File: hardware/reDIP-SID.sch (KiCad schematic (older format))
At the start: 72 parts, among them J1 Conn_01x01, J2 Conn_01x05, J3 Conn_01x14, J4 Conn_01x10, J5 TYPE-C-31-M-12, J6 Conn_02x05_Odd_Even, SW1 KXT311LHS, U1 NCP115AMX120TCG, U10 W25Q128JVPIM, U11 ICE40UP5K-SG48I, U2 NCP167AMX330TBG, U3 NCP115AMX120TCG, U4 FPF1321UCX, U5 SN74CBTD16211DGVR, U6 SGTL5000XNLA3, U7 NUF2042XV6, U8 MCP6H01T-E/OT, U9 LY68L6400SLIT, X1 ASCO-24.000MHZ-EK-T3

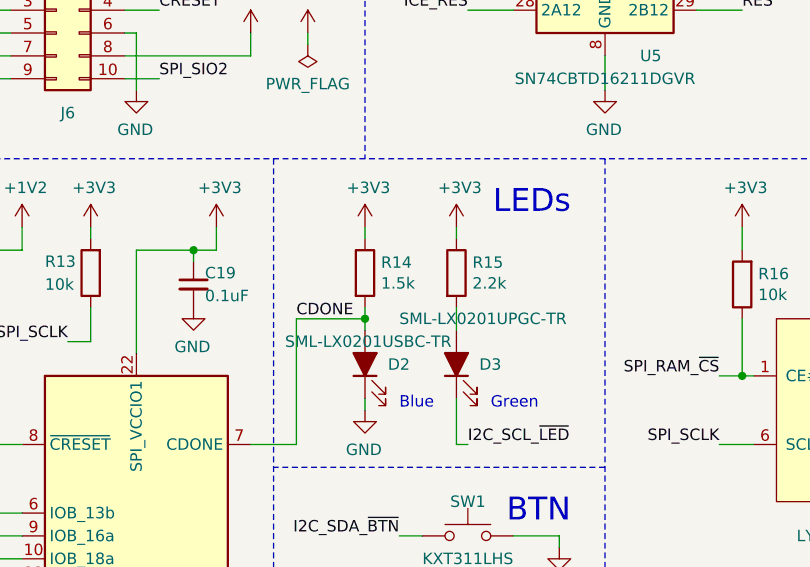
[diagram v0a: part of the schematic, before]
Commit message: Minor updates
* Dimmer blue CDONE LED
* BOM QA
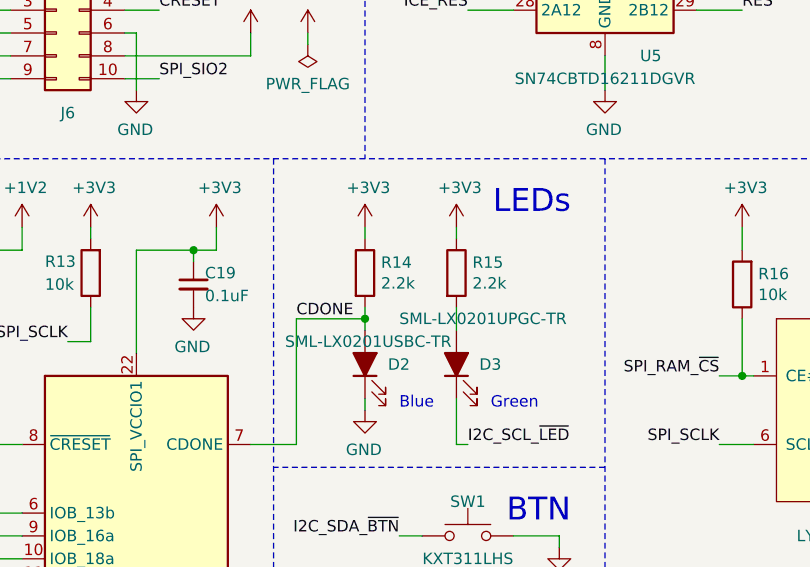
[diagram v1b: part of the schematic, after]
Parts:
- R14: value 1.5k -> 2.2k; Description RES 1.5kΩ 50mW 5% 0201 -> RES 2.2kΩ 50mW 5% 0201; PN ERJ-1GNJ152C -> ERJ-1GNJ222C
- R20: Description RES 22Ω 50mW 5% 0201 -> RES 22Ω 50mW 1% 0201; PN ERJ-1GNJ220C -> ERJ-1GNF22R0C
- SW1: Description SW TACT 3.0 x 2.0 mm -> SW TACT 100gf 3.0x2.0 mm
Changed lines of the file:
@@
 F 1 "W25Q128JVPIM" H 10200 5000 50  0000 C CNN
 F 2 "Package_SON:WSON-8-1EP_6x5mm_P1.27mm_EP3.4x4.3mm" H 10200 5600 50  0001 C CNN
-F 3 "https://www.winbond.com/resource-files/w25q128jv%20revf%2003272018%20plus.pdf" H 10200 5600 50  0001 C CNN
+F 3 "https://www.winbond.com/resource-files/W25Q128JV%20RevH%2003102021%20Plus.pdf" H 10200 5600 50  0001 C CNN
 F 4 "IC FLASH 128Mbit WSON-8" H 10200 5600 50  0001 C CNN "Description"
 F 5 "Winbond" H 10200 5600 50  0001 C CNN "Mfg"
@@
 P 5900 5050
 F 0 "R14" H 5970 5096 50  0000 L CNN
-F 1 "1.5k" H 5970 5005 50  0000 L CNN
+F 1 "2.2k" H 5970 5005 50  0000 L CNN
 F 2 "Resistor_SMD:R_0201_0603Metric" V 5830 5050 50  0001 C CNN
-F 3 "https://industrial.panasonic.com/ww/products/pt/general-purpose-chip-resistors/models/ERJ1GNJ152C" H 5900 5050 50  0001 C CNN
-F 4 "RES 1.5kΩ 50mW 5% 0201" H 5900 5050 50  0001 C CNN "Description"
+F 3 "https://industrial.panasonic.com/ww/products/pt/general-purpose-chip-resistors/models/ERJ1GNJ222C" H 5900 5050 50  0001 C CNN
+F 4 "RES 2.2kΩ 50mW 5% 0201" H 5900 5050 50  0001 C CNN "Description"
 F 5 "Panasonic" H 5900 5050 50  0001 C CNN "Mfg"
-F 6 "ERJ-1GNJ152C" H 5900 5050 50  0001 C CNN "PN"
+F 6 "ERJ-1GNJ222C" H 5900 5050 50  0001 C CNN "PN"
 	1    5900 5050
 	1    0    0    -1
@@
 F 1 "Conn_02x05_Odd_Even" H 4600 4326 50  0001 C CNN
 F 2 "reDIP:PinHeader_2x05_P2.54mm_Vertical" H 4550 4000 50  0001 C CNN
-F 3 "https://drawings-pdf.s3.amazonaws.com/11636.pdf" H 4550 4000 50  0001 C CNN
+F 3 "" H 4550 4000 50  0001 C CNN
 F 4 "CONN HDR SQ PIN 2x5 POS .100\" GOLD MATING 6mm TAIL 3mm" H 4550 4000 50  0001 C CNN "Description"
 F 5 "" H 4550 4000 50  0001 C CNN "Mfg"
@@
 F 1 "NCP167AMX330TBG" H 4050 1374 50  0000 C CNN
 F 2 "ONSemi:CASE_711AJ_1.0x1.0mm_P0.65mm" H 4050 1100 50  0001 C CNN
-F 3 "https://www.onsemi.com/pub/Collateral/NCP167-D.PDF" H 4050 1100 50  0001 C CNN
+F 3 "https://www.onsemi.com/pdf/datasheet/ncp167-d.pdf" H 4050 1100 50  0001 C CNN
 F 4 "onsemi" H 4050 1100 50  0001 C CNN "Mfg"
 F 5 "NCP167AMX330TBG" H 4050 1100 50  0001 C CNN "PN"
@@
 F 2 "CK:SW_SPST_CK_KXT3" H 6350 6400 50  0001 C CNN
 F 3 "https://www.ckswitches.com/media/1465/kxt3.pdf" H 6350 6400 50  0001 C CNN
-F 4 "SW TACT 3.0 x 2.0 mm" H 6350 6200 50  0001 C CNN "Description"
+F 4 "SW TACT 100gf 3.0x2.0 mm" H 6350 6200 50  0001 C CNN "Description"
 F 5 "C&K" H 6350 6200 50  0001 C CNN "Mfg"
 F 6 "KXT311LHS" H 6350 6200 50  0001 C CNN "PN"
@@
 F 1 "22" V 4200 7400 50  0000 C CNN
 F 2 "Resistor_SMD:R_0201_0603Metric" H 4250 7300 50  0001 C CNN
-F 3 "https://industrial.panasonic.com/ww/products/pt/general-purpose-chip-resistors/models/ERJ1GNJ220C" H 4250 7300 50  0001 C CNN
+F 3 "https://industrial.panasonic.com/ww/products/pt/general-purpose-chip-resistors/models/ERJ1GNF22R0C" H 4250 7300 50  0001 C CNN
 F 4 "Panasonic" H 4250 7300 50  0001 C CNN "Mfg"
-F 5 "ERJ-1GNJ220C" H 4250 7300 50  0001 C CNN "PN"
-F 6 "RES 22Ω 50mW 5% 0201" H 4250 7300 50  0001 C CNN "Description"
+F 5 "ERJ-1GNF22R0C" H 4250 7300 50  0001 C CNN "PN"
+F 6 "RES 22Ω 50mW 1% 0201" H 4250 7300 50  0001 C CNN "Description"
 	1    4250 7300
 	0    1    1    0
@@
 F 1 "NUF2042XV6" H 2600 2800 50  0000 C CNN
 F 2 "ONSemi:CASE_463A_1.6x1.2mm_P0.5mm" H 2600 2750 50  0001 C CNN
-F 3 "https://www.onsemi.com/pub/Collateral/NUF2030XV6-D.PDF" H 2800 3600 50  0001 C CNN
+F 3 "https://www.onsemi.com/pdf/datasheet/nuf2030xv6-d.pdf" H 2800 3600 50  0001 C CNN
 F 4 "IC USB TERMINATOR ESD PROTECTION SOT-563" H 2600 3250 50  0001 C CNN "Description"
 F 5 "onsemi" H 2600 3250 50  0001 C CNN "Mfg"

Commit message: Tweaks before manufacture
* Added test point for 5V rail
* Got rid of one BOM line by changing the MIC voltage divider
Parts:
- removed TP1, TP2: TestPoint_Flag, reDIP:TestPoint_Pad_D0.75mm, symbol Connector:TestPoint_Flag
- added TP1, TP2, TP3: TestPoint, reDIP:TestPoint_Pad_D0.75mm, symbol Connector:TestPoint
- R5: value 402k -> 100k; Description RES 402kΩ 50mW 1% 0201 -> RES 100kΩ 50mW 1% 0201; PN ERJ-1GNF4023C -> ERJ-1GNF1003C
- R8: value 100k -> 20k; Description RES 100kΩ 50mW 1% 0201 -> RES 20kΩ 50mW 1% 0201; PN ERJ-1GNF1003C -> ERJ-1GNF2002C
- renumbered TP3 to TP4, TP4 to TP5
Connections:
- net +1V2: now also TP2.1
- net +5V: now also TP1.1
- net VDDD: now also TP3.1
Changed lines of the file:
@@
 Sheet 1 1
 Title "reDIP SID"
-Date "2021-08-28"
+Date "2021-09-07"
 Rev "1.0"
 Comp "Nimrod"
@@
 $EndComp
 $Comp
-L Connector:TestPoint_Flag TP4
+L Connector:TestPoint_Flag TP5
 U 1 1 5EBD10F6
 P 10700 1650
-F 0 "TP4" H 10960 1698 50  0000 L CNN
+F 0 "TP5" H 10960 1698 50  0000 L CNN
 F 1 "TestPoint_Flag" H 10960 1653 50  0001 L CNN
 F 2 "reDIP:TestPoint_Pad_D0.75mm" H 10900 1650 50  0001 C CNN
@@
 $EndComp
 $Comp
-L Connector:TestPoint_Flag TP3
+L Connector:TestPoint_Flag TP4
 U 1 1 5EA8BEE8
 P 10700 1500
-F 0 "TP3" H 10960 1548 50  0000 L CNN
+F 0 "TP4" H 10960 1548 50  0000 L CNN
 F 1 "TestPoint_Flag" H 10960 1503 50  0001 L CNN
 F 2 "reDIP:TestPoint_Pad_D0.75mm" H 10900 1500 50  0001 C CNN
@@
 Power
 Wire Wire Line
-	3250 1000 3250 800
+	3250 1000 3250 850
 Wire Wire Line
 	4550 1000 4550 800
@@
 Wire Wire Line
 	3950 3450 3950 3500
-Wire Wire Line
-	3150 1200 3250 1200
 $Comp
 L Device:C_Small C4
@@
 Connection ~ 5750 6850
 Wire Wire Line
-	5600 1000 5600 800
+	5600 1000 5600 850
 Wire Wire Line
 	5500 1000 5600 1000
@@
 Connection ~ 4750 1000
 $Comp
-L Connector:TestPoint_Flag TP2
-U 1 1 615B5C23
-P 5600 1200
-F 0 "TP2" H 5850 1200 50  0000 R CNN
-F 1 "TestPoint_Flag" H 5860 1203 50  0001 L CNN
-F 2 "reDIP:TestPoint_Pad_D0.75mm" H 5800 1200 50  0001 C CNN
-F 3 "~" H 5800 1200 50  0001 C CNN
-F 4 "PAD" H 5600 1200 50  0001 C CNN "DNP"
-	1    5600 1200
-	1    0    0    1
-$EndComp
-$Comp
 L Device:C_Small C8
 U 1 1 615B5C31
@@
 	1    0    0    -1
 $EndComp
-$Comp
-L Connector:TestPoint_Flag TP1
-U 1 1 5F4F3F1B
-P 3250 1200
-F 0 "TP1" H 3500 1200 50  0000 R CNN
-F 1 "TestPoint_Flag" H 3510 1203 50  0001 L CNN
-F 2 "reDIP:TestPoint_Pad_D0.75mm" H 3450 1200 50  0001 C CNN
-F 3 "~" H 3450 1200 50  0001 C CNN
-F 4 "PAD" H 3250 1200 50  0001 C CNN "DNP"
-	1    3250 1200
-	1    0    0    1
-$EndComp
 Wire Wire Line
 	3150 1000 3150 1100
@@
 	3150 1100 3150 1200
 Connection ~ 4550 1000
-Connection ~ 3150 1200
 Wire Wire Line
 	8250 1450 8250 1500
@@
 	5500 1000 5500 1200
 Wire Wire Line
-	5600 1200 5500 1200
-Connection ~ 5500 1200
-Wire Wire Line
 	10100 3500 10100 3750
 Wire Wire Line
@@
 	1450 1300 1450 1450
 Wire Wire Line
-	2200 800  2200 1000
+	2200 800  2200 850
 $Comp
 L Device:R R5
@@
 P 8450 2600
 F 0 "R5" V 8400 2500 50  0000 R CNN
-F 1 "402k" V 8400 2900 50  0000 R CNN
+F 1 "100k" V 8400 2900 50  0000 R CNN
 F 2 "Resistor_SMD:R_0201_0603Metric" V 8380 2600 50  0001 C CNN
-F 3 "https://industrial.panasonic.com/ww/products/pt/general-purpose-chip-resistors/models/ERJ1GNF4023C" H 8450 2600 50  0001 C CNN
+F 3 "https://industrial.panasonic.com/ww/products/pt/general-purpose-chip-resistors/models/ERJ1GNF1003C" H 8450 2600 50  0001 C CNN
 F 4 "Panasonic" H 8450 2600 50  0001 C CNN "Mfg"
-F 5 "ERJ-1GNF4023C" H 8450 2600 50  0001 C CNN "PN"
-F 6 "RES 402kΩ 50mW 1% 0201" H 8450 2600 50  0001 C CNN "Description"
+F 5 "ERJ-1GNF1003C" H 8450 2600 50  0001 C CNN "PN"
+F 6 "RES 100kΩ 50mW 1% 0201" H 8450 2600 50  0001 C CNN "Description"
 	1    8450 2600
 	0    1    1    0
@@
 P 8450 2750
 F 0 "R8" V 8400 2650 50  0000 R CNN
-F 1 "100k" V 8400 3050 50  0000 R CNN
+F 1 "20k" V 8400 3050 50  0000 R CNN
 F 2 "Resistor_SMD:R_0201_0603Metric" V 8380 2750 50  0001 C CNN
-F 3 "https://industrial.panasonic.com/ww/products/pt/general-purpose-chip-resistors/models/ERJ1GNF1003C" H 8450 2750 50  0001 C CNN
+F 3 "https://industrial.panasonic.com/ww/products/pt/general-purpose-chip-resistors/models/ERJ1GNF2002C" H 8450 2750 50  0001 C CNN
 F 4 "Panasonic" H 8450 2750 50  0001 C CNN "Mfg"
-F 5 "ERJ-1GNF1003C" H 8450 2750 50  0001 C CNN "PN"
-F 6 "RES 100kΩ 50mW 1% 0201" H 8450 2750 50  0001 C CNN "Description"
+F 5 "ERJ-1GNF2002C" H 8450 2750 50  0001 C CNN "PN"
+F 6 "RES 20kΩ 50mW 1% 0201" H 8450 2750 50  0001 C CNN "Description"
 	1    8450 2750
 	0    1    1    0
@@
 Wire Wire Line
 	2200 4950 2400 4950
+Connection ~ 2200 850
+Wire Wire Line
+	2200 850  2200 1000
+Connection ~ 3250 850
+Wire Wire Line
+	3250 850  3250 800
+Connection ~ 5600 850
+Wire Wire Line
+	5600 850  5600 800
+$Comp
+L Connector:TestPoint TP1
+U 1 1 61417994
+P 2200 850
+F 0 "TP1" V 2100 900 50  0000 L CNN
+F 1 "TestPoint" V 2245 1038 50  0001 L CNN
+F 2 "reDIP:TestPoint_Pad_D0.75mm" H 2400 850 50  0001 C CNN
+F 3 "~" H 2400 850 50  0001 C CNN
+	1    2200 850
+	0    1    1    0
+$EndComp
+$Comp
+L Connector:TestPoint TP2
+U 1 1 614195BB
+P 3250 850
+F 0 "TP2" V 3150 900 50  0000 L CNN
+F 1 "TestPoint" V 3295 1038 50  0001 L CNN
+F 2 "reDIP:TestPoint_Pad_D0.75mm" H 3450 850 50  0001 C CNN
+F 3 "~" H 3450 850 50  0001 C CNN
+	1    3250 850
+	0    1    1    0
+$EndComp
+$Comp
+L Connector:TestPoint TP3
+U 1 1 6141A62A
+P 5600 850
+F 0 "TP3" V 5500 900 50  0000 L CNN
+F 1 "TestPoint" V 5645 1038 50  0001 L CNN
+F 2 "reDIP:TestPoint_Pad_D0.75mm" H 5800 850 50  0001 C CNN
+F 3 "~" H 5800 850 50  0001 C CNN
+	1    5600 850
+	0    1    1    0
+$EndComp
 $EndSCHEMATC

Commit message: Made all test points equal
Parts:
- TP4, TP5: symbol Connector:TestPoint_Flag -> Connector:TestPoint
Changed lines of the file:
@@
 $EndComp
 $Comp
-L Connector:TestPoint_Flag TP5
-U 1 1 5EBD10F6
-P 10700 1650
-F 0 "TP5" H 10960 1698 50  0000 L CNN
-F 1 "TestPoint_Flag" H 10960 1653 50  0001 L CNN
-F 2 "reDIP:TestPoint_Pad_D0.75mm" H 10900 1650 50  0001 C CNN
-F 3 "~" H 10900 1650 50  0001 C CNN
-F 4 "PAD" H 10700 1650 50  0001 C CNN "DNP"
-	1    10700 1650
-	1    0    0    -1
-$EndComp
-$Comp
-L Connector:TestPoint_Flag TP4
-U 1 1 5EA8BEE8
-P 10700 1500
-F 0 "TP4" H 10960 1548 50  0000 L CNN
-F 1 "TestPoint_Flag" H 10960 1503 50  0001 L CNN
-F 2 "reDIP:TestPoint_Pad_D0.75mm" H 10900 1500 50  0001 C CNN
-F 3 "~" H 10900 1500 50  0001 C CNN
-F 4 "PAD" H 10700 1500 50  0001 C CNN "DNP"
-	1    10700 1500
-	1    0    0    -1
-$EndComp
-$Comp
 L Device:C_Small C11
 U 1 1 5EC6D44C
@@
 Connection ~ 10300 1650
 Wire Wire Line
-	10300 1650 10700 1650
-Wire Wire Line
 	10550 1350 10550 1500
 Connection ~ 10550 1500
-Wire Wire Line
-	10550 1500 10700 1500
 Text Notes 10300 850  0    50   ~ 0
 I2C Pullup
@@
 	0    1    1    0
 $EndComp
+Wire Wire Line
+	10300 1650 10700 1650
+$Comp
+L Connector:TestPoint TP5
+U 1 1 5EBD10F6
+P 10700 1650
+F 0 "TP5" V 10700 1850 50  0000 L CNN
+F 1 "TestPoint_Flag" H 10960 1653 50  0001 L CNN
+F 2 "reDIP:TestPoint_Pad_D0.75mm" H 10900 1650 50  0001 C CNN
+F 3 "~" H 10900 1650 50  0001 C CNN
+F 4 "PAD" H 10700 1650 50  0001 C CNN "DNP"
+	1    10700 1650
+	0    1    1    0
+$EndComp
+Wire Wire Line
+	10550 1500 10700 1500
+$Comp
+L Connector:TestPoint TP4
+U 1 1 5EA8BEE8
+P 10700 1500
+F 0 "TP4" V 10700 1700 50  0000 L CNN
+F 1 "TestPoint_Flag" H 10960 1503 50  0001 L CNN
+F 2 "reDIP:TestPoint_Pad_D0.75mm" H 10900 1500 50  0001 C CNN
+F 3 "~" H 10900 1500 50  0001 C CNN
+F 4 "PAD" H 10700 1500 50  0001 C CNN "DNP"
+	1    10700 1500
+	0    1    1    0
+$EndComp

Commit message: Modified ESD protection footprint to accomodate other SOT-563 / SOT-666 devices
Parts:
- U7: footprint ONSemi:CASE_463A_1.6x1.2mm_P0.5mm -> reDIP:SOT-563
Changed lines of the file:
@@
 Sheet 1 1
 Title "reDIP SID"
-Date "2021-09-07"
+Date "2021-09-14"
 Rev "1.0"
 Comp "Nimrod"
@@
 F 0 "U7" H 2850 3650 50  0000 C CNN
 F 1 "NUF2042XV6" H 2600 2800 50  0000 C CNN
-F 2 "ONSemi:CASE_463A_1.6x1.2mm_P0.5mm" H 2600 2750 50  0001 C CNN
+F 2 "reDIP:SOT-563" H 2600 2750 50  0001 C CNN
 F 3 "https://www.onsemi.com/pdf/datasheet/nuf2030xv6-d.pdf" H 2800 3600 50  0001 C CNN
 F 4 "IC USB TERMINATOR ESD PROTECTION SOT-563" H 2600 3250 50  0001 C CNN "Description"
